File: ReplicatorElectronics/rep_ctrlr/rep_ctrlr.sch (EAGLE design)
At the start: 86 parts, among them IC1 MICROCHIP_PIC32MX7X5F256L-PF, IC2 MICROCHIP_MCP6001-LT, IC3 MICROCHIP_MCP6001-LT, IC4 MICROCHIP_MCP6001-LT, IC5 MICROCHIP_MCP6001-LT, IC6 LT1963E-3.3Q, J1 ATX24RH, J10 SBH21-NBPN-D05-ST-BK, J11 SBH21-NBPN-D07-ST-BK, J12 SBH21-NBPN-D07-ST-BK, J13 SBH21-NBPN-D07-ST-BK, J14 SBH21-NBPN-D07-ST-BK, J15 SBH21-NBPN-D07-ST-BK, J3 FPS009-30003, J4 SBH21-NBPN-D05-ST-BK, J5 SBH21-NBPN-D05-ST-BK, J6 SBH21-NBPN-D07-ST-BK, J7 SBH21-NBPN-D07-ST-BK, J8 SBH21-NBPN-D05-ST-BK, J9 SBH21-NBPN-D07-ST-BK, X1 CMR3XXT, X2 CMR3XXT

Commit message: 3/4/12: Rev. 4 Controller. Completed PHY, replaced placeholder connectors for PRG header and spool with real ones, swapped out 3.3V LDO with in-stock component of different package type, replaced 2mm connectors with 0.100" connectors.
Note: 25 MHz crystal is a non-stock item in that family, needs replacement in Rev. 5.
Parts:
- removed IC6: LT1963E-3.3Q, linear-technology:LT1963E-3.3Q
- removed J5: SBH21-NBPN-D05-ST-BK, SBH21-NBPN-D05-ST-BK:SBH21-NBPN-D05-ST-BK
- removed JP1: (no value), SparkFun-Connectors:M06POLAR
- added C24, C25, C26, C27: 0.1uF, resistor:C-USC0603
- added C28, C29: 1uF, resistor:C-USC0603
- added C30: 0.1uF, rcl:C-USC0603
- added IC7: LT1963AEQ-3.3, linear-technology:LT1963AEQ-3.3
- added J16, J17: SBH11-PBPC-D07-ST-BK, SBH11-PBPC-D07-ST-BK:SBH11-PBPC-D07-ST-BK
- added J18: SI-50170-F, con-stewart:SI-50170
- added J19: 70553-0106, 70553-0109:70553-0106
- added R37, R38, R39, R40: 49.9, resistor:R-US_R0603
- added R41, R42: 270, resistor:R-US_R0603
- added R43: FERRITE, resistor:R-US_R0805
- added R44, R45: 10k, resistor:R-US_R0603
- J10: value SBH21-NBPN-D05-ST-BK -> SBH11-PBPC-D07-ST-BK; device SBH21-NBPN-D05-ST-BK:SBH21-NBPN-D05-ST-BK -> SBH11-PBPC-D07-ST-BK:SBH11-PBPC-D07-ST-BK
- J11, J12, J13, J14, J15: value SBH21-NBPN-D07-ST-BK -> SBH11-PBPC-D07-ST-BK; device SBH21-NBPN-D07-ST-BK:SBH21-NBPN-D07-ST-BK -> SBH11-PBPC-D07-ST-BK:SBH11-PBPC-D07-ST-BK
- J3: value FPS009-30003 -> FPS009-3003
- J4: value SBH21-NBPN-D05-ST-BK -> RJ11-2L-B; device SBH21-NBPN-D05-ST-BK:SBH21-NBPN-D05-ST-BK -> con-tycoelectronics:RJ11-2L-B
- J6, J7, J9: value SBH21-NBPN-D07-ST-BK -> SBH11-PBPC-D05-ST-BK; device SBH21-NBPN-D07-ST-BK:SBH21-NBPN-D07-ST-BK -> SBH11-PBPC-D05-ST-BK:SBH11-PBPC-D05-ST-BK
- J8: value SBH21-NBPN-D05-ST-BK -> SBH11-PBPC-D05-ST-BK; device SBH21-NBPN-D05-ST-BK:SBH21-NBPN-D05-ST-BK -> SBH11-PBPC-D05-ST-BK:SBH11-PBPC-D05-ST-BK
- R25, R26, R27, R28, R29, R30, R31, R32, R33, R34, R35: value 10 -> 50
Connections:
- removed net ETDX0: R26.1
- removed net ETDX1: R25.1
- new net EMDC: IC1PD.EMDC/AEMDC/IC4/PMCS1/PMA14/RD11, R34.1
- new net ETH_3_3V: C26.1, C27.1, C28.1, J18.RCT, J18.TCT, R37.2, R38.2, R39.2, R40.2, R43.1, U$2G$2.VDD1A, U$2G$2.VDD2A
- new net ETXD0: IC1PD.AETXD0/SS1A/U1BRX/U1ACTS/CN20/RD14, R26.1
- new net ETXD1: IC1PD.AETXD1/SCK1A/U1BTX/U1ARTS/CN21/RD15, R25.1
- new net ETXERR: IC1PB.AN11/ERXERR/AETXERR/PMA12/RB11
- new net N$22: C29.1
- new net N$42: J18.C, R42.2
- new net N$43: J18.C1, R41.2
- new net N$44: C29.2, U$2G$2.VDDCR
- new net PS_ON: IC1PD.PMRD/CN14/RD5, J1.PS_ON
- net 12V_HEAT: now also J6.1, J6.3, J6.5, J7.1, J7.3, J7.5, J9.1, J9.3, J9.5; no longer J10.1, J10.3, J10.5, J4.1, J4.3, J4.5, J5.1, J5.3, J5.5
- net 5V_SERVO: now also J10.1, J10.3, J10.5, J16.1, J16.3, J16.5, J17.1, J17.3, J17.5; no longer J6.1, J6.3, J6.5, J7.1, J7.3, J7.5, J9.1, J9.3, J9.5
- net 5V_USB: now also IC7.!SHDN, IC7.IN; no longer IC6.!SHDN, IC6.IN
- net DGND: now also C24.2, C25.2, C26.2, C27.2, C28.2, C30.2, IC7.GND, IC7.GND@1, J18.C_GND, J18.S1, J18.S2, J4.3, R41.1, R42.1, R44.1, R45.1, U$2G$2.VSS; no longer IC6.GND, J11.10, J11.12, J12.10, J12.12, J13.10, J13.12, J14.10, J14.12, J15.10, J15.12, J6.10, J6.12, J7.10, J7.12, J9.10, J9.12, JP1.1
- net ECRSDV: now also IC1PG.SCL2A/SDO2A/U2ATX/PMA3/CN10/RG8, R31.1; no longer R32.1
- net EMDIO: now also IC1PD.RTCC/EMDIO/AEMDIO/IC1/RD8, R33.1; no longer R34.1
- net ENC0_CSN: now also J10.7; no longer J9.7
- net ENC1_CSN: now also J11.7; no longer J6.7
- net ENC2_CSN: now also J12.7; no longer J11.7
- net ENC3_CSN: now also J13.7; no longer J7.7
- net ENC4_CSN: now also J14.7; no longer J12.7
- net ENC5_CSN: now also J15.7; no longer J13.7
- net ENC6_CSN: now also J16.7; no longer J14.7
- net ENC7_CSN: now also J17.7; no longer J15.7
- net ENC_3_3V: now also C24.1, C25.1, R43.2, U$2G$2.VDDIO; no longer J11.14, J12.14, J13.14, J14.14, J15.14, J6.14, J7.14, J9.14
- net ENC_MISO: now also J10.13, J16.13, J17.13; no longer J6.13, J7.13, J9.13
- net ENC_MOSI: now also J10.11, J16.11, J17.11; no longer J6.11, J7.11, J9.11
- net ENC_SCK: now also J10.9, J16.9, J17.9; no longer J6.9, J7.9, J9.9
- net EREFCLK: now also IC1PG.SS2A/U2BRX/U2ACTS/PMA2/CN11/RG9, R32.1; no longer R33.1
- net ERXD0: now also IC1PE.AERXD0/INT1/RE8
- net ERXD1: now also IC1PE.AERXD1/INT2/RE9
- net ERXERR: now also IC1PG.AERXERR/RG15, R30.1; no longer R31.1
- net GND: now also J6.8, J7.8, J9.8; no longer J10.2, J10.4, J10.6, J10.8, J11.2, J11.4, J11.6, J12.2, J12.4, J12.6, J13.2, J13.4, J13.6, J14.2, J14.4, J14.6, J15.2, J15.4, J15.6, J4.2, J4.4, J4.6, J4.8, J5.2, J5.4, J5.6, J5.8
- net HEAT0_ON: now also J6.7; no longer IC1PG.SS2A/U2BRX/U2ACTS/PMA2/CN11/RG9, J8.7
- net HEAT1_ON: now also J7.7; no longer J5.7
- net HEAT2_ON: now also J8.7; no longer J10.7
- net HEAT3_ON: now also J9.7; no longer J4.7
- net LED1: now also J18.A
- net LED2: now also J18.A1, R45.2
- net MCLRN: now also J4.1
- net N$11: now also J9.9; no longer J4.9
- net N$12: now also J9.10; no longer J4.10
- net N$13: now also J7.10; no longer J5.10
- net N$16: now also J6.9; no longer J8.9
- net N$17: now also J6.10; no longer J8.10
- net N$19: now also J8.9; no longer J10.9
- net N$20: now also J8.10; no longer J10.10
- net N$33: now also R44.2
- net N$34: now also J18.TD+, R37.1
- net N$35: now also J18.TD-, R38.1
- net N$36: now also J18.RD+, R39.1
- net N$37: now also J18.RD-, R40.1
- net N$9: now also J7.9; no longer J5.9
- net NRST: now also IC1PG.ECOL/SCK2A/U2BTXU2ARTS/PMA5/CN8/RG6
- net PGEC: now also J4.5
- net SD_SP_MISO: no longer JP1.4
- net SD_SP_MOSI: no longer JP1.3
- net SD_SP_SCK: no longer JP1.6
- net SERVO0: no longer J9.8
- net SERVO1: no longer J6.8
- net SERVO2: no longer J11.8
- net SERVO3: no longer J7.8
- net SERVO4: no longer J12.8
- net SERVO5: no longer J13.8
- net SERVO6: no longer J14.8
- net SERVO7: no longer J15.8
- net SP_CSN: no longer JP1.5
- net VCC: now also IC7.OUT, IC7.SENSE, J4.2; no longer IC6.SENSE, JP1.2
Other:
- note removed: "ADD ZENERS"
- note removed: "EXT OSCILLATOR?"
- note removed: "INSERT 3.3V LDO HERE"
- note removed: "LIKELY CHOICE"
- note removed: "NEED CONNECTOR FOR SPOOL SPI. PLACEHOLDER USED."
- note removed: "NEED PROGRAMMING HDR"
- moved on the sheet: J11, J12, J13, J14, J15, J8

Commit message: rough layout demo
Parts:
- removed C20, C21: 4.7uF, resistor:C-USC0603
- removed IC7: LT1963AEQ-3.3, linear-technology:LT1963AEQ-3.3
- added 3.3V, 5V: PTR1TP14R, testpad:PTR1TP14R
- added C31, C32: 4.7uF, rcl:CPOL-USR/2012-12R
- added C33: .1uF, rcl:C-USC0402
- added R46: 10k, rcl:R-US_R0402
- added U18: LDS3985XX33, LDS3985XX33:LDS3985XX33
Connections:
- new net +3V3: 3.3V.TP, C31.+, U18.VOUT
- new net 5V: 5V.TP, C32.+, R46.1, U18.VIN
- new net N$40: R46.2, U18.EN
- new net N$41: C33.1, U18.BYPASS
- net 5V_USB: no longer C21.1, IC7.!SHDN, IC7.IN
- net DGND: no longer C20.2, C21.2, IC7.GND, IC7.GND@1
- net GND: now also C31.-, C32.-, C33.2, U18.GND
- net VCC: no longer C20.1, IC7.OUT, IC7.SENSE
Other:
- note added: "3.3v LDO"
- note removed: "AC: Added LDO"

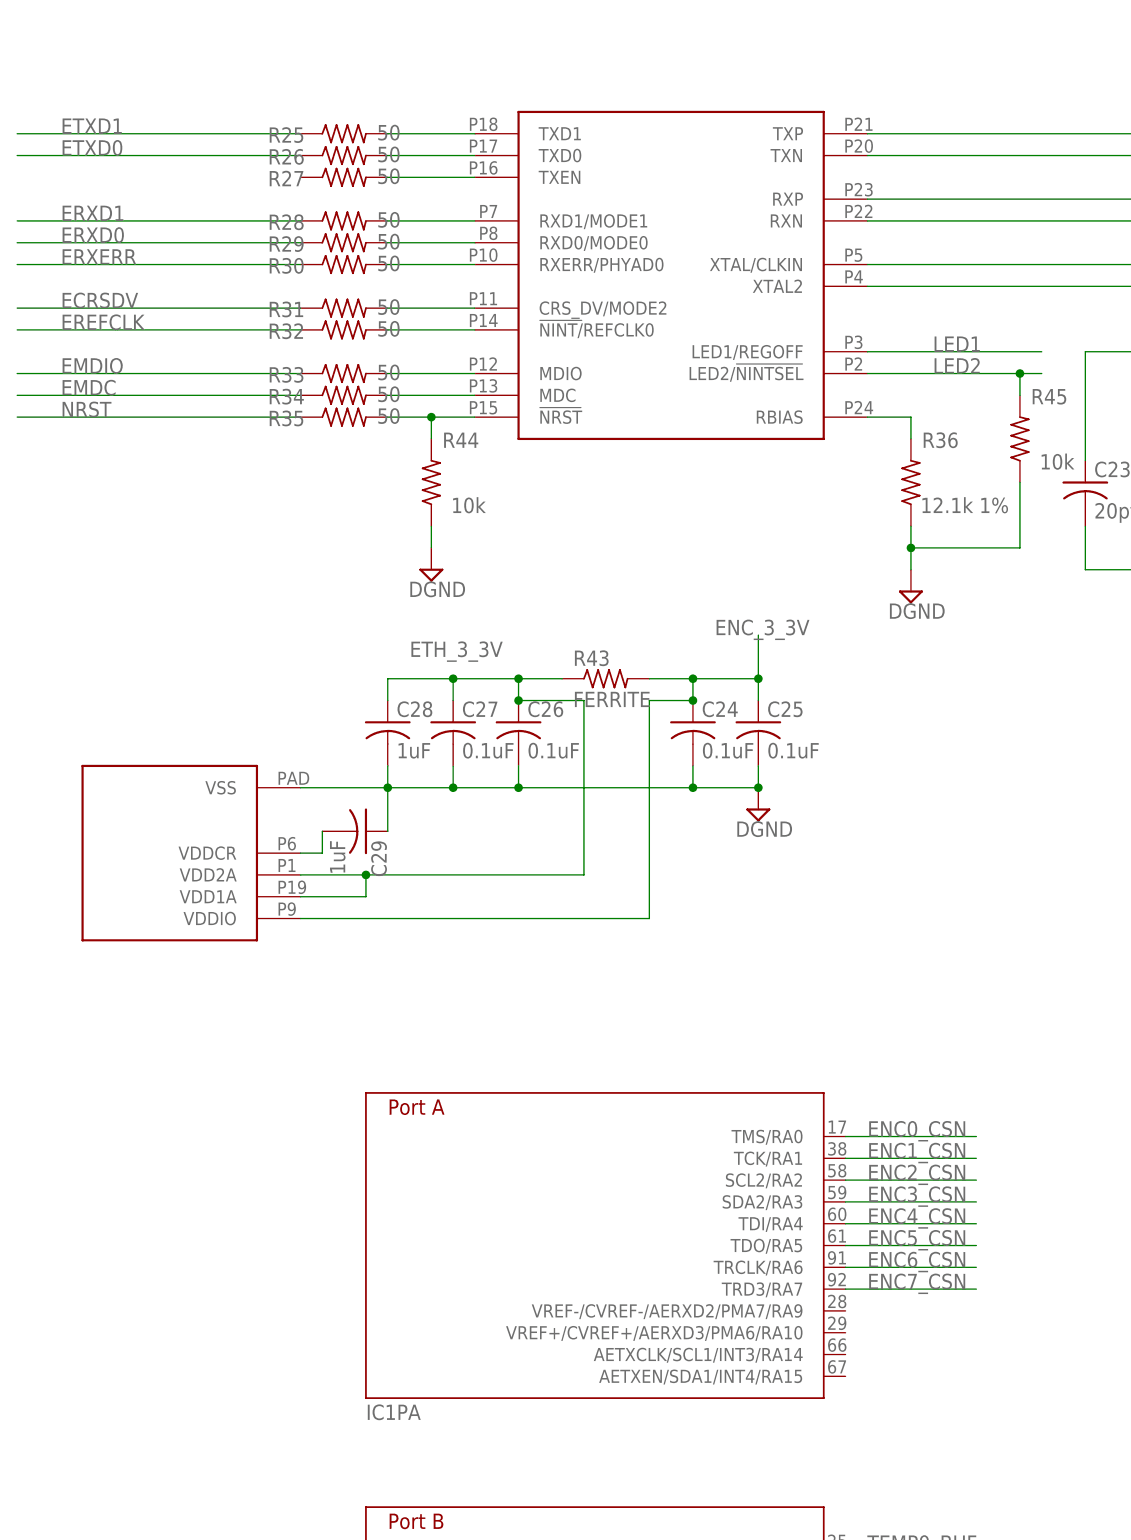
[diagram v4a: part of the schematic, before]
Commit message: 5/5/12: Routed good portion of the PHY. Work in progress.
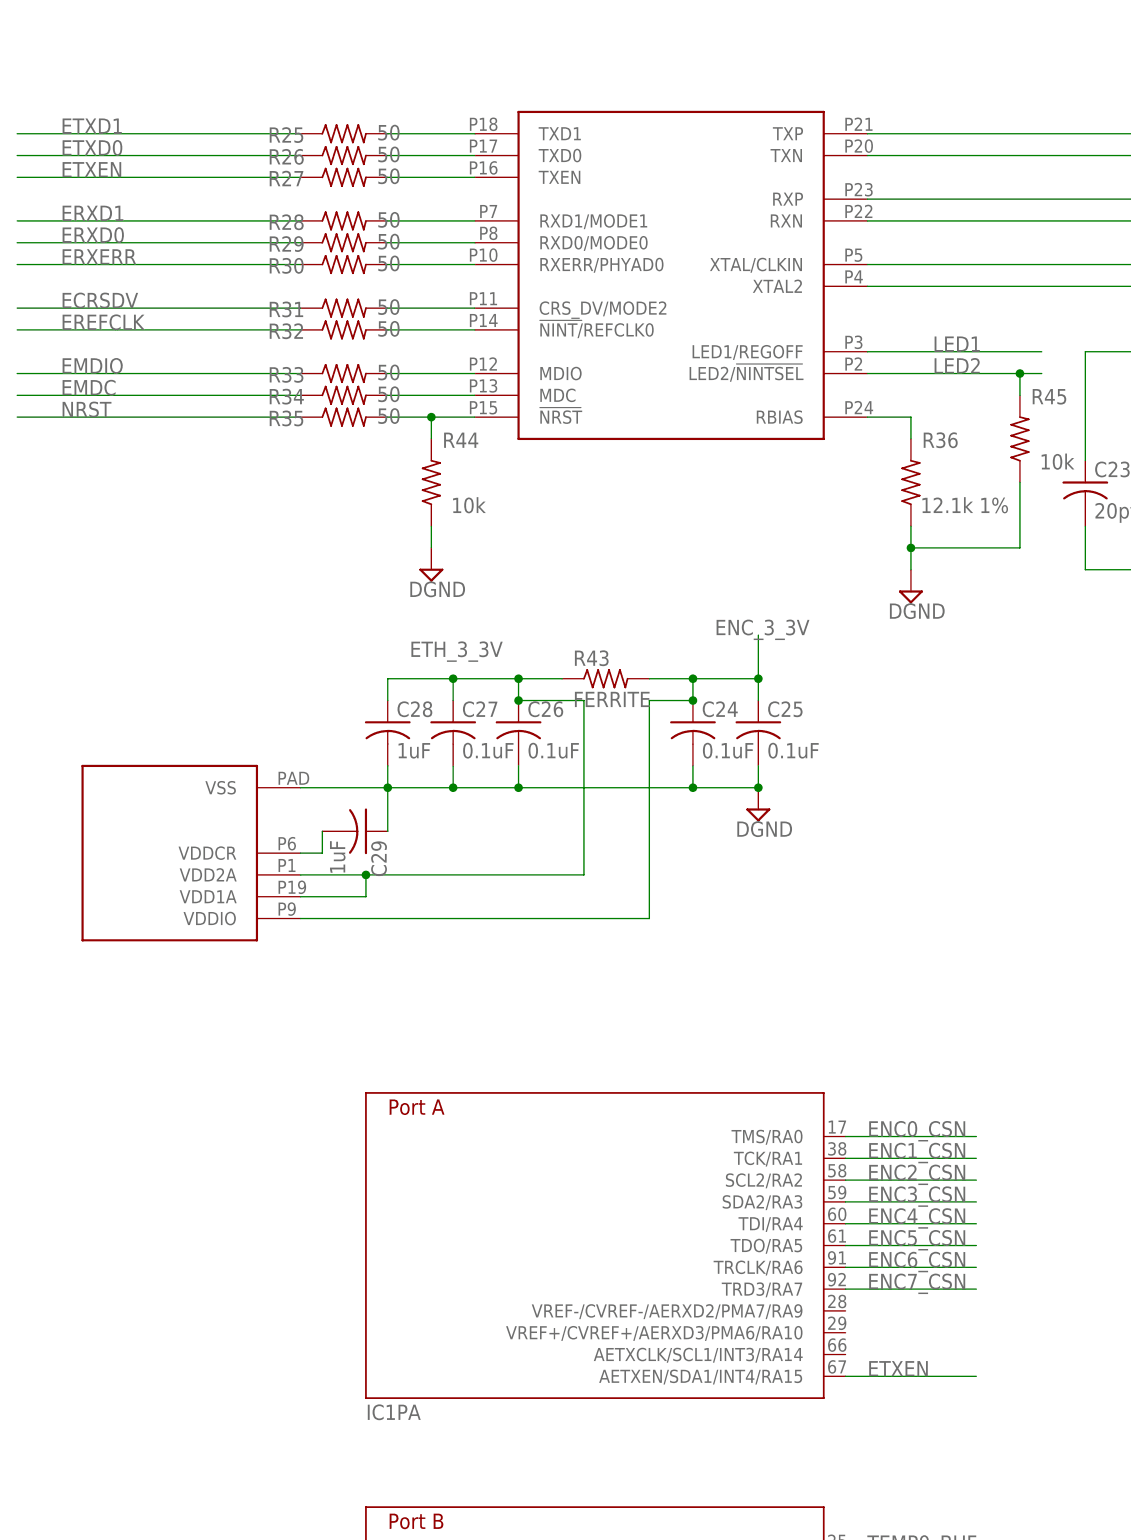
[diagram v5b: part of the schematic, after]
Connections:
- removed net N$22: C29.1
- new net ETXEN: IC1PA.AETXEN/SDA1/INT4/RA15, R27.1
- net DGND: now also C29.1
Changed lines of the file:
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@@
 <pinref part="SUPPLY42" gate="G$1" pin="DGND"/>
 <junction x="-73.66" y="15.24"/>
+<pinref part="C29" gate="G$1" pin="1"/>
+<wire x1="-116.84" y1="10.16" x2="-116.84" y2="15.24" width="0.1524" layer="91"/>
 </segment>
 <segment>
@@
 </segment>
 </net>
-<net name="N$22" class="0">
-<segment>
-<pinref part="C29" gate="G$1" pin="1"/>
-<wire x1="-116.84" y1="15.24" x2="-116.84" y2="10.16" width="0.1524" layer="91"/>
-</segment>
-</net>
 <net name="5V" class="0">
 <segment>
@@
 </segment>
 </net>
+<net name="ETXEN" class="0">
+<segment>
+<pinref part="R27" gate="G$1" pin="1"/>
+<wire x1="-127" y1="86.36" x2="-160.02" y2="86.36" width="0.1524" layer="91"/>
+<label x="-154.94" y="86.36" size="1.778" layer="95"/>
+</segment>
+<segment>
+<pinref part="IC1" gate="PA" pin="AETXEN/SDA1/INT4/RA15"/>
+<wire x1="-63.5" y1="-53.34" x2="-48.26" y2="-53.34" width="0.1524" layer="91"/>
+<label x="-60.96" y="-53.34" size="1.778" layer="95"/>
+</segment>
+</net>

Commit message: 5/8/12: First complete PHY layout attempt. Other parts of board still require routing.
~ 2 hrs.
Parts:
- removed Q1: (no value), semicon-smd-ipc:NPN-TRANSISTOR_SOT23
- removed R10, R11, R12, R9: 22, resistor:R-US_R0603
- removed U$1: PETERATMEGA644_LCD37, microtouch:PETERATMEGA644_LCD37
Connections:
- removed net LCD_LED: Q1.B
- removed net N$1: R9.2, U$1.LEDK1
- removed net N$10: Q1.C, R10.1, R11.1, R12.1, R9.1
- removed net N$3: R10.2, U$1.LEDK2
- removed net N$4: R11.2, U$1.LEDK3
- removed net N$6: R12.2, U$1.LEDK4
- new net N$54: IC1PD.ETXD2/IC5/PMD12/RD12
- new net N$55: IC1PD.ETXD3/PMD13/CN19/RD13
- net A0: no longer U$1.RS(A0)
- net DB0: no longer U$1.DB0
- net DB1: no longer U$1.DB1
- net DB10: no longer U$1.DB10
- net DB11: no longer U$1.DB11
- net DB14: no longer IC1PD.ETXD2/IC5/PMD12/RD12, U$1.DB12
- net DB15: no longer IC1PD.ETXD3/PMD13/CN19/RD13, U$1.DB13
- net DB16: no longer U$1.DB14, U$1.DB16
- net DB17: no longer U$1.DB15, U$1.DB17
- net DB2: no longer U$1.DB2
- net DB3: no longer U$1.DB3
- net DB4: no longer U$1.DB4
- net DB5: no longer U$1.DB5
- net DB6: no longer U$1.DB6
- net DB7: no longer U$1.DB7
- net DGND: now also J10.10, J10.12, J11.10, J11.12, J12.10, J12.12, J13.10, J13.12, J14.10, J14.12, J15.10, J15.12, J16.10, J16.12, J17.10, J17.12; no longer Q1.E, U$1.GND@1, U$1.GND@2, U$1.NC@1, U$1.NC@2
- net ENC_3_3V: now also J10.14, J11.14, J12.14, J13.14, J14.14, J15.14, J16.14, J17.14
- net GND: now also J10.2, J10.4, J10.6, J11.2, J11.4, J11.6, J12.2, J12.4, J12.6, J13.2, J13.4, J13.6, J14.2, J14.4, J14.6, J15.2, J15.4, J15.6, J16.2, J16.4, J16.6, J17.2, J17.4, J17.6
- net LCD_CS: no longer U$1.CS
- net LCD_RD: no longer U$1.RD
- net LCD_RST: no longer U$1.RESET
- net LCD_WR: no longer U$1.WR
- net SERVO0: now also J10.8
- net SERVO1: now also J11.8
- net SERVO2: now also J12.8
- net SERVO3: now also J13.8
- net SERVO4: now also J14.8
- net SERVO5: now also J15.8
- net SERVO6: now also J16.8
- net SERVO7: now also J17.8
- net VCC: no longer U$1.LEDA, U$1.VCC@1, U$1.VCC@2, U$1.VCI
- net X+: no longer U$1.X+
- net X-: no longer U$1.X-
- net Y+: no longer U$1.Y+
- net Y-: no longer U$1.Y-

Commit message: 5/13/12: More PIC Routing
~5 hrs.
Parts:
- removed C22, C23: 20pf, rcl:C-USC0603
- removed J3: FPS009-3003, con-yamaichi:FPS009-30003
- removed R3, R4, R5, R6, R7: 50k, resistor:R-US_R0603
- removed X1, X2: CMR3XXT, cmr3XXT:CMR3XXT
- added Q1, Q2: ASFL1, crystal:ASFL1
- added R10, R9: 10, resistor:R-US_R0603
- C18: value 20pf -> 0.1u; device rcl:C-USC0603 -> resistor:C-USC0603
- C19: value 20pf -> 0.1uF
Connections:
- removed net 5V: 5V.TP, C32.+, R46.1, U18.VIN
- removed net N$39: C23.1, U$2G$1.XTAL2, X1.P$1
- removed net N$7: J3.8, R4.1
- removed net N$8: J3.9, R3.1
- new net N$1: Q2.FO, R9.2
- new net N$4: Q1.FO, R10.2
- net 5V_USB: now also 5V.TP, C32.+, R46.1, U18.VIN
- net DGND: now also C18.2, C19.2, C31.-, C32.-, C33.2, J1.GND@0, J1.GND@1, J1.GND@2, J1.GND@3, J1.GND@4, J1.GND@5, J1.GND@6, J1.GND@7, J19.6, Q1.GND, Q2.GND, U18.GND; no longer C22.2, C23.2, J3.3, J3.6, X1.SHIELD
- net GND: no longer C18.2, C19.2, C31.-, C32.-, C33.2, J1.GND@0, J1.GND@1, J1.GND@2, J1.GND@3, J1.GND@4, J1.GND@5, J1.GND@6, J1.GND@7, U18.GND
- net N$38: now also R10.1; no longer C22.1, X1.P$2
- net PICCLKI: now also R9.1; no longer C18.1, X2.P$1
- net PICCLKO: no longer C19.1, X2.P$2
- net SD_CSN: no longer J3.1, R7.1
- net SD_SP_MISO: now also J19.3; no longer J3.7, R5.1
- net SD_SP_MOSI: now also J19.4; no longer J3.2, R6.1
- net SD_SP_SCK: now also J19.1; no longer J3.5
- net SP_CSN: now also J19.2
- net VCC: now also C18.1, C19.1, J19.5, Q1.VCC, Q2.VCC; no longer J3.4, R3.2, R4.2, R5.2, R6.2, R7.2
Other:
- moved on the sheet: C18, C19

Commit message: 5/13/12: Added level translator, added LCD board connector. Corrected connector widths - this required ripup of most traces associated with them. Began new attempt at PIC routing which should be more orderly and compact.
~ 3 hrs.
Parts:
- added U$1: SBH11-PBPC-D13-ST-BK, SBH11-PBPC-D13-ST-BK:SBH11-PBPC-D13-ST-BK
- added U$3: SN74ACT244, SN74ACT244:SN74ACT244
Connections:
- removed net N$54: IC1PD.ETXD2/IC5/PMD12/RD12
- removed net N$55: IC1PD.ETXD3/PMD13/CN19/RD13
- new net DB12: IC1PF.C1TX/ETXD0/PMD10/RF1, U$1.12
- new net DB13: IC1PF.C1RX/ETXD1/PMD11/RF0, U$1.13
- new net SERVO0_5V: U$3.1Y1
- new net SERVO1_5V: U$3.1Y2
- new net SERVO2_5V: U$3.1Y3
- new net SERVO3_5V: U$3.1Y4
- new net SERVO4_5V: U$3.2Y1
- new net SERVO5_5V: U$3.2Y2
- new net SERVO6_5V: U$3.2Y3
- new net SERVO7_5V: U$3.2Y4
- net 5V_USB: now also U$3.VCC
- net A0: now also U$1.1
- net DB0: now also U$1.2
- net DB1: now also U$1.3
- net DB10: now also U$1.10
- net DB11: now also U$1.11
- net DB14: now also IC1PD.ETXD2/IC5/PMD12/RD12, U$1.14; no longer IC1PF.C1TX/ETXD0/PMD10/RF1
- net DB15: now also IC1PD.ETXD3/PMD13/CN19/RD13, U$1.15; no longer IC1PF.C1RX/ETXD1/PMD11/RF0
- net DB16: now also U$1.16
- net DB17: now also U$1.17
- net DB2: now also U$1.4
- net DB3: now also U$1.5
- net DB4: now also U$1.6
- net DB5: now also U$1.7
- net DB6: now also U$1.8
- net DB7: now also U$1.9
- net DGND: now also U$1.22, U$1.24, U$1.26, U$3.1OEN, U$3.2OEN, U$3.GND
- net PGED: now also J4.4
- net SD_CSN: now also U$1.18
- net SD_SP_MISO: now also U$1.20
- net SD_SP_MOSI: now also U$1.21
- net SD_SP_SCK: now also U$1.19
- net SERVO0: now also U$3.1A1
- net SERVO1: now also U$3.1A2
- net SERVO2: now also U$3.1A3
- net SERVO3: now also U$3.1A4
- net SERVO4: now also U$3.2A1
- net SERVO5: now also U$3.2A2
- net SERVO6: now also U$3.2A3
- net SERVO7: now also U$3.2A4
- net VCC: now also U$1.23, U$1.25
